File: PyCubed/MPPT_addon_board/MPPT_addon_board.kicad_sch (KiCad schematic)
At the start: 16 parts, among them J1 HW-09-10-L-D-400-SM, Q9 MBT2222ADW1T1, U1 LT8491-mezzanine, U2 LT8491-mezzanine

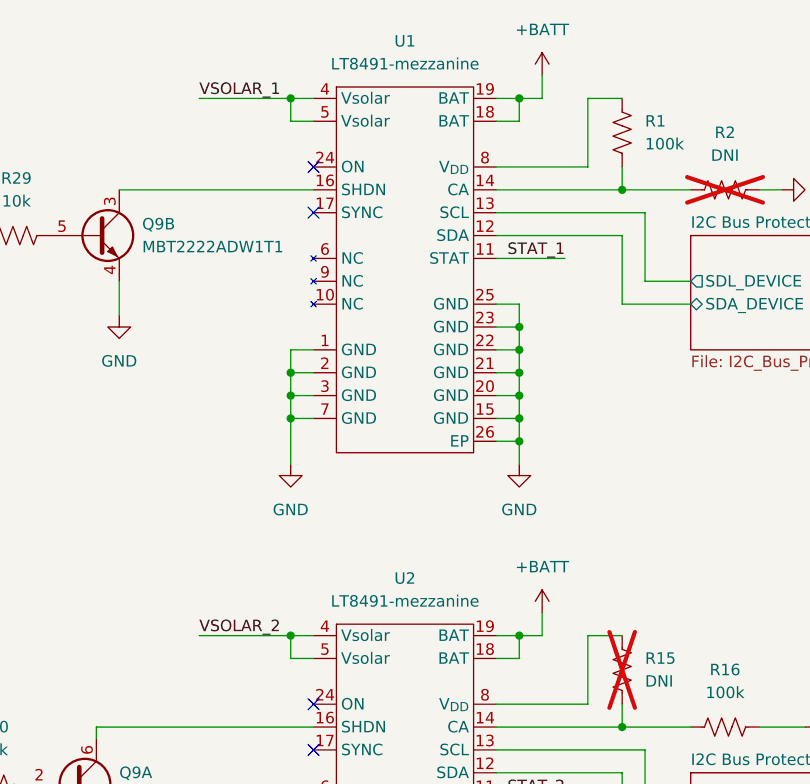
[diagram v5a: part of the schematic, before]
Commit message: updated MPPT add-on to kicad v08
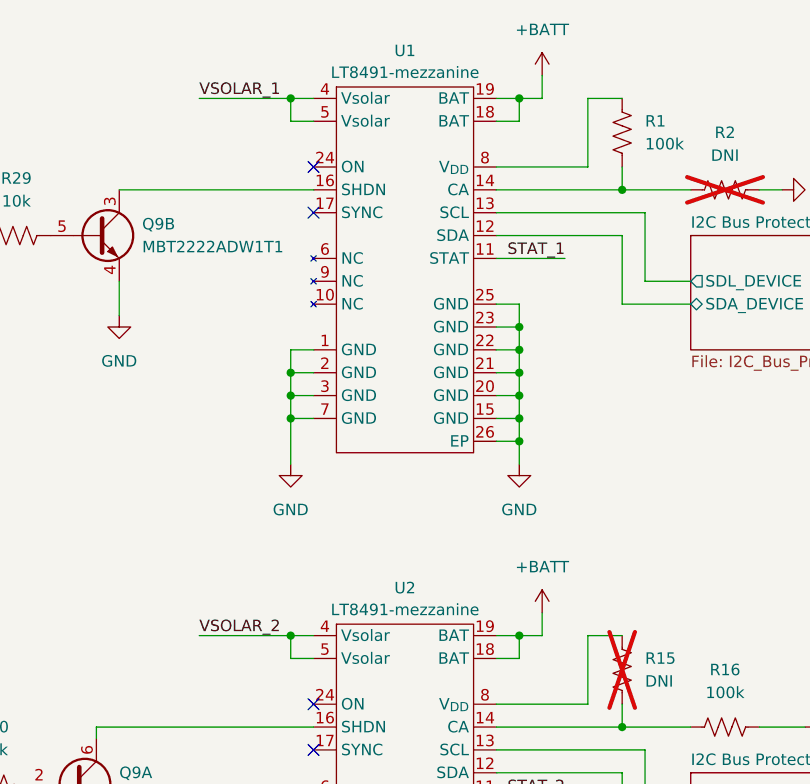
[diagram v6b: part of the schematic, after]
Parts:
- J1: footprint mainboard:SAMTEC_HW-09-XX-X-D-XXX-SM-A -> ssi_connector:SAMTEC_HW-09-XX-X-D-XXX-SM-A; symbol mainboard:HW-09-10-L-D-400-SM -> ssi_connector:HW-09-10-L-D-400-SM
- R15, R2: now in the parts list
- U1, U2: footprint mainboard:LT8491-mezzanine -> ssi_IC:LT8491-mezzanine; symbol mainboard:MPPT_module -> ssi_IC:MPPT_module
